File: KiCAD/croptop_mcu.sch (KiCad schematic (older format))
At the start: 46 parts

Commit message: Updates ESD protection diodes
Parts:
- removed TP?: TestPoint, symbol Connector:TestPoint
- added C17: 10uF, Capacitor_SMD:C_0805_2012Metric, symbol Device:C
- added FID1: FIDUCIAL, Fiducial:Fiducial_0.75mm_Dia_1.5mm_Outer, symbol CropTop:FIDUCIAL
- added FID2: FIDUCIAL, symbol CropTop:FIDUCIAL
- added H1: Top Left, symbol Mechanical:MountingHole
- added H2: Bottom Left, symbol Mechanical:MountingHole
- added H3: Top Right, symbol Mechanical:MountingHole
- added H4: Bottom Right, symbol Mechanical:MountingHole
- added R68, R69: 10, Resistor_SMD:R_0402_1005Metric, symbol Device:R
- added R70: 0, Resistor_SMD:R_0402_1005Metric, symbol Device:R
- added U16: PUSBM5V5X4, symbol CropTop:PUSBM5V5X4
- C1, C10, C11, C12, C13, C3, C4, C6, C7, C8, C9: renamed from C?; footprint (none) -> Capacitor_SMD:C_0402_1005Metric
- C2, C5: renamed from C?; footprint (none) -> Capacitor_SMD:C_0805_2012Metric
- R1, R10, R11, R12, R13, R14, R15, R16, R17, R18, R19, R2, R20, R21, R22, R23, R24, R25, R26, R27, R3, R4, R5, R6, R7, R8, R9: renamed from R?; footprint (none) -> Resistor_SMD:R_0402_1005Metric
- U1: renamed from U?; footprint MODULE -> Package_QFP:TQFP-100_12x12mm_P0.4mm
- gave numbers to parts that had none: 4
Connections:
- net labels added: ADC_CS, DVDD_UNREG, MISO, MOSI, RX, SCL, SCLK, SDA, TX
- net labels removed: GPS_RX, GPS_TX, MISO_1, MOSI_1, SCLK_1, SCL_1, SDA_1
- wire segments 248 -> 268
- no-connect marks 8 -> 12
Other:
- note added: "Mounting Holes & Fiducials"
- note removed: "Possibly\nD.N.P."
- note removed: "Supply \nmust\nbe 5V\nnot 3V3"
- moved on the sheet: C1, J1, J2, R1

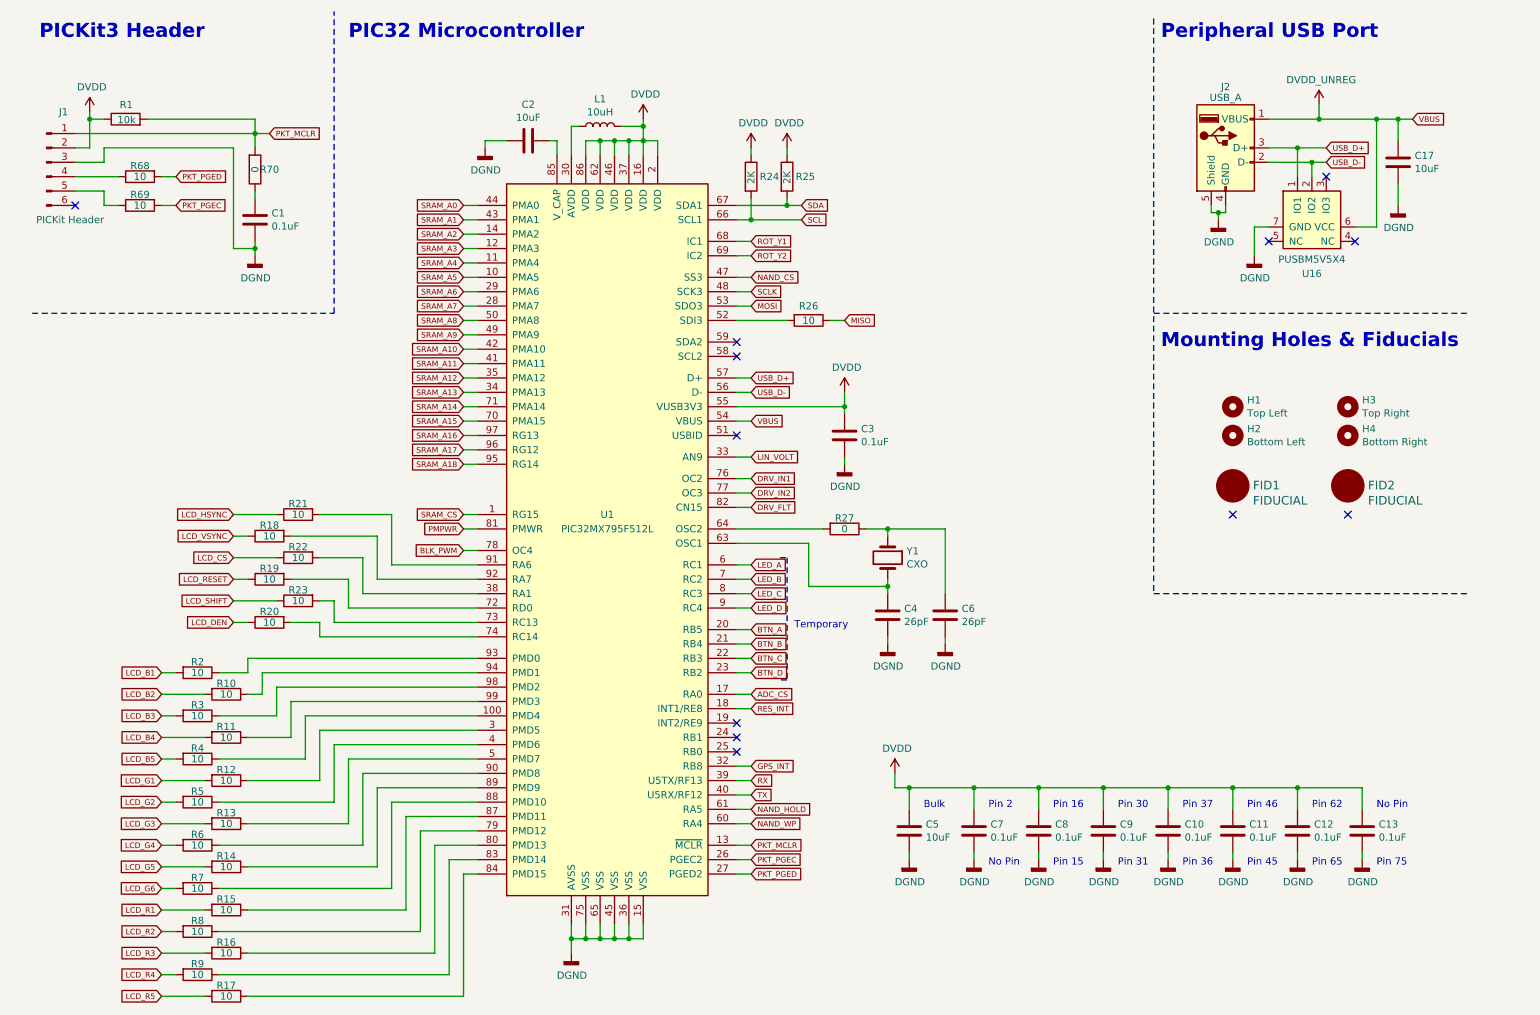
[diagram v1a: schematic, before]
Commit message: Got to PCB layout
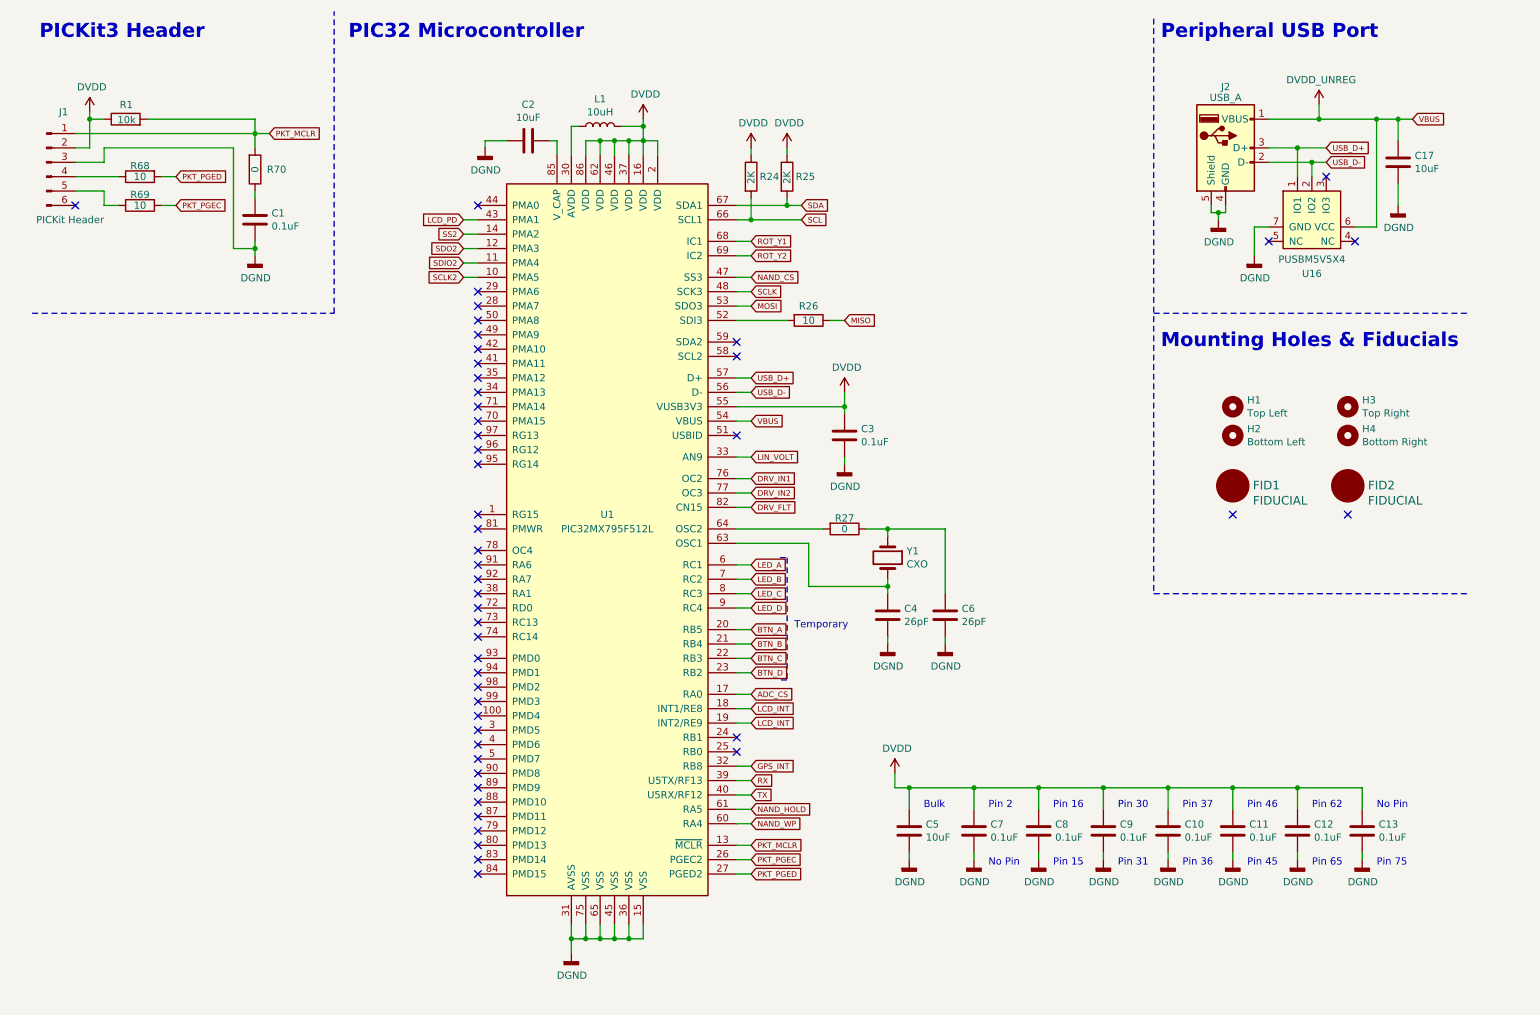
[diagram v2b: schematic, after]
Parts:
- removed R10, R11, R12, R13, R14, R15, R16, R17, R18, R19, R2, R20, R21, R22, R23, R3, R4, R5, R6, R7, R8, R9: 10, Resistor_SMD:R_0402_1005Metric, symbol Device:R
- FID1: footprint Fiducial:Fiducial_0.75mm_Dia_1.5mm_Outer -> Fiducial:Fiducial_1mm_Dia_2.54mm_Outer_CopperTop
- FID2: footprint (none) -> Fiducial:Fiducial_1mm_Dia_2.54mm_Outer_CopperTop
- H1, H2, H3, H4: footprint (none) -> MountingHole:MountingHole_4mm
- J1: footprint (none) -> Connector_PinHeader_2.54mm:PinHeader_1x06_P2.54mm_Vertical
- J2: footprint (none) -> croptop:USB_A_Assmann_Horizontal
- L1: footprint (none) -> Inductor_SMD:L_1210_3225Metric
- U16: footprint (none) -> croptop:PUSBM5V5X4
- Y1: footprint (none) -> croptop:ABLS_OX
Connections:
- net RES_INT is gone; now on net LCD_INT: U1.18 (INT1/RE8)
- net LCD_INT: now reaches U1.19 (INT2/RE9)
- net BLK_PWM: no longer names the net of U1.78 (OC4)
- net PMPWR: no longer names the net of U1.81 (PMWR)
- net SRAM_A0: no longer names the net of U1.44 (PMA0)
- net SRAM_A1 renamed LCD_PD
- net SRAM_A10: no longer names the net of U1.42 (PMA10)
- net SRAM_A11: no longer names the net of U1.41 (PMA11)
- net SRAM_A12: no longer names the net of U1.35 (PMA12)
- net SRAM_A13: no longer names the net of U1.34 (PMA13)
- net SRAM_A14: no longer names the net of U1.71 (PMA14)
- net SRAM_A15: no longer names the net of U1.70 (PMA15)
- net SRAM_A16: no longer names the net of U1.97 (RG13)
- net SRAM_A17: no longer names the net of U1.96 (RG12)
- net SRAM_A18: no longer names the net of U1.95 (RG14)
- net SRAM_A2 renamed SS2
- net SRAM_A3 renamed SDO2
- net SRAM_A4 renamed SDIO2
- net SRAM_A5 renamed SCLK2
- net SRAM_A6: no longer names the net of U1.29 (PMA6)
- net SRAM_A7: no longer names the net of U1.28 (PMA7)
- net SRAM_A8: no longer names the net of U1.50 (PMA8)
- net SRAM_A9: no longer names the net of U1.49 (PMA9)
- net SRAM_CS: no longer names the net of U1.1 (RG15)
- no-connect marks 12 -> 50

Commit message: Before remove LCD resistors
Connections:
- net BTN_C: no longer names the net of U1.22 (RB3)
- net BTN_D: no longer names the net of U1.23 (RB2)
- no-connect marks 50 -> 52
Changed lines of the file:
@@
 Text GLabel 5500 4900 2    39   Input ~ 0
 BTN_B
-Text GLabel 5500 5000 2    39   Input ~ 0
-BTN_C
-Text GLabel 5500 5100 2    39   Input ~ 0
-BTN_D
 Text GLabel 5500 4350 2    39   Input ~ 0
 LED_A
@@
 Wire Wire Line
 	5500 4900 5400 4900
-Wire Wire Line
-	5500 5000 5400 5000
-Wire Wire Line
-	5500 5100 5400 5100
 Wire Wire Line
 	5500 1800 5500 1950
@@
 Wire Wire Line
 	5400 5450 5500 5450
+NoConn ~ 5400 5000
+NoConn ~ 5400 5100
 $EndSCHEMATC

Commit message: Finished working board
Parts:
- removed R68, R69: 10, Resistor_SMD:R_0402_1005Metric, symbol Device:R
- H1, H2, H3, H4: footprint MountingHole:MountingHole_4mm -> MountingHole:MountingHole_4mm_Pad
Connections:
- net BTN_A: now also U1.74 (RC14); no longer U1.20 (RB5)
- net BTN_B: now also U1.73 (RC13); no longer U1.21 (RB4)
- net GPS_INT: now also U1.19 (INT2/RE9); no longer U1.32 (RB8)
- net LCD_INT: no longer U1.19 (INT2/RE9)
- net PKT_PGEC: now also J1.5 (Pin_5)
- net PKT_PGED: now also J1.4 (Pin_4)
- net LED_C: no longer names the net of U1.8 (RC3)
- net LED_D: no longer names the net of U1.9 (RC4)
- no-connect marks 52 -> 55
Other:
- note removed: "Temporary"
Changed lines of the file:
@@
 Wire Wire Line
 	4150 1400 4100 1400
-Text GLabel 5500 4800 2    39   Input ~ 0
+Text GLabel 3500 4850 0    39   Input ~ 0
 BTN_A
-Text GLabel 5500 4900 2    39   Input ~ 0
+Text GLabel 3500 4750 0    39   Input ~ 0
 BTN_B
 Text GLabel 5500 4350 2    39   Input ~ 0
@@
 Text GLabel 5500 4450 2    39   Input ~ 0
 LED_B
-Text GLabel 5500 4550 2    39   Input ~ 0
-LED_C
-Text GLabel 5500 4650 2    39   Input ~ 0
-LED_D
 $Comp
 L Device:R R?
@@
 	5400 2550 5500 2550
 Wire Wire Line
-	5500 4650 5400 4650
-Wire Wire Line
-	5500 4550 5400 4550
-Wire Wire Line
 	5500 4450 5400 4450
 Wire Wire Line
 	5500 4350 5400 4350
-Wire Wire Line
-	5500 4800 5400 4800
-Wire Wire Line
-	5500 4900 5400 4900
 Wire Wire Line
 	5500 1800 5500 1950
@@
 Wire Wire Line
 	6450 4100 6850 4100
-Text GLabel 10100 1250 2    39   Input ~ 0
-VBUS
-Text GLabel 5500 3350 2    39   Input ~ 0
-VBUS
-Wire Wire Line
-	5400 3350 5500 3350
 Wire Wire Line
 	6150 3150 6150 3250
@@
 Wire Wire Line
 	6050 2650 6150 2650
-Text GLabel 5500 5750 2    39   Input ~ 0
+Text GLabel 5500 5450 2    39   Input ~ 0
 GPS_INT
 Wire Wire Line
-	5400 5750 5500 5750
+	5400 5450 5500 5450
 Wire Wire Line
 	6300 4100 6450 4100
@@
 Text Notes 550  700  0    98   ~ 20
 PICKit3 Header
-Wire Notes Line
-	5700 4300 5750 4300
-Wire Notes Line
-	5750 4300 5750 5150
-Wire Notes Line
-	5750 5150 5700 5150
-Text Notes 5800 4800 0    50   ~ 0
-Temporary
 Wire Wire Line
 	9750 6350 9750 6400
@@
 F 0 "H1" H 8950 3296 50  0000 L CNN
 F 1 "Top Left" H 8950 3205 50  0000 L CNN
-F 2 "MountingHole:MountingHole_4mm" H 8850 3250 50  0001 C CNN
+F 2 "MountingHole:MountingHole_4mm_Pad" H 8850 3250 50  0001 C CNN
 F 3 "~" H 8850 3250 50  0001 C CNN
 	1    8850 3250
@@
 F 0 "H3" H 9750 3296 50  0000 L CNN
 F 1 "Top Right" H 9750 3205 50  0000 L CNN
-F 2 "MountingHole:MountingHole_4mm" H 9650 3250 50  0001 C CNN
+F 2 "MountingHole:MountingHole_4mm_Pad" H 9650 3250 50  0001 C CNN
 F 3 "~" H 9650 3250 50  0001 C CNN
 	1    9650 3250
@@
 F 0 "H2" H 8950 3496 50  0000 L CNN
 F 1 "Bottom Left" H 8950 3405 50  0000 L CNN
-F 2 "MountingHole:MountingHole_4mm" H 8850 3450 50  0001 C CNN
+F 2 "MountingHole:MountingHole_4mm_Pad" H 8850 3450 50  0001 C CNN
 F 3 "~" H 8850 3450 50  0001 C CNN
 	1    8850 3450
@@
 F 0 "H4" H 9750 3496 50  0000 L CNN
 F 1 "Bottom Right" H 9750 3405 50  0000 L CNN
-F 2 "MountingHole:MountingHole_4mm" H 9650 3450 50  0001 C CNN
+F 2 "MountingHole:MountingHole_4mm_Pad" H 9650 3450 50  0001 C CNN
 F 3 "~" H 9650 3450 50  0001 C CNN
 	1    9650 3450
@@
 NoConn ~ 8850 4000
 NoConn ~ 9650 4000
-$Comp
-L Device:R R?
-U 1 1 5C0298E7
-P 1250 1650
-AR Path="/5C0298E7" Ref="R?"  Part="1"
-AR Path="/64807BBC/5C0298E7" Ref="R68"  Part="1"
-F 0 "R68" V 1175 1650 50  0000 C CNN
-F 1 "10" V 1250 1650 50  0000 C CNN
-F 2 "Resistor_SMD:R_0402_1005Metric" V 1180 1650 50  0001 C CNN
-F 3 "~" H 1250 1650 50  0001 C CNN
-	1    1250 1650
-	0    -1   1    0
-$EndComp
-$Comp
-L Device:R R?
-U 1 1 5C08DA6B
-P 1250 1850
-AR Path="/5C08DA6B" Ref="R?"  Part="1"
-AR Path="/64807BBC/5C08DA6B" Ref="R69"  Part="1"
-F 0 "R69" V 1175 1850 50  0000 C CNN
-F 1 "10" V 1250 1850 50  0000 C CNN
-F 2 "Resistor_SMD:R_0402_1005Metric" V 1180 1850 50  0001 C CNN
-F 3 "~" H 1250 1850 50  0001 C CNN
-	1    1250 1850
-	0    -1   1    0
-$EndComp
 Wire Wire Line
 	800  1550 1000 1550
@@
 	1000 1550 1000 1450
 Wire Wire Line
-	800  1650 1100 1650
-Wire Wire Line
 	1000 1750 1000 1850
 Wire Wire Line
-	1000 1850 1100 1850
-Wire Wire Line
 	800  1750 1000 1750
 Wire Wire Line
@@
 Wire Wire Line
 	800  1350 2050 1350
-Wire Wire Line
-	1400 1650 1500 1650
-Wire Wire Line
-	1400 1850 1500 1850
 $Comp
 L Device:R R?
@@
 Wire Wire Line
 	10000 1400 10000 1250
-Connection ~ 10000 1250
-Wire Wire Line
-	10000 1250 10100 1250
 Wire Wire Line
 	10000 1700 10000 1850
@@
 NoConn ~ 3600 5100
 NoConn ~ 3600 5000
-NoConn ~ 3600 4850
-NoConn ~ 3600 4750
 NoConn ~ 3600 4650
 NoConn ~ 3600 4550
@@
 NoConn ~ 3600 2450
 NoConn ~ 3600 1850
-Text GLabel 5500 5450 2    39   Input ~ 0
-LCD_INT
 Text GLabel 3500 1950 0    39   Input ~ 0
 LCD_PD
 Wire Wire Line
 	3500 1950 3600 1950
-Wire Wire Line
-	5400 5450 5500 5450
 NoConn ~ 5400 5000
 NoConn ~ 5400 5100
+Wire Wire Line
+	800  1650 1500 1650
+Wire Wire Line
+	1000 1850 1500 1850
+NoConn ~ 5400 5750
+NoConn ~ 5400 4650
+NoConn ~ 5400 4550
+NoConn ~ 5400 4900
+NoConn ~ 5400 4800
+Wire Wire Line
+	3500 4750 3600 4750
+Wire Wire Line
+	3500 4850 3600 4850
+$Comp
+L CropTop:DVDD_UNREG #PWR?
+U 1 1 5C31543C
+P 5900 3000
+AR Path="/64809F0C/5C31543C" Ref="#PWR?"  Part="1"
+AR Path="/64807BBC/5C31543C" Ref="#PWR?"  Part="1"
+F 0 "#PWR?" H 5900 2850 50  0001 C CNN
+F 1 "DVDD_UNREG" H 5915 3173 50  0000 C CNN
+F 2 "" H 5900 3000 50  0001 C CNN
+F 3 "" H 5900 3000 50  0001 C CNN
+	1    5900 3000
+	1    0    0    -1
+$EndComp
+Wire Wire Line
+	5400 3350 5900 3350
+Wire Wire Line
+	5900 3350 5900 3000
 $EndSCHEMATC

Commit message: Complete PCB version 1
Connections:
- no-connect marks 55 -> 53
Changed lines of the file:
@@
 Wire Wire Line
 	5500 5250 5400 5250
-NoConn ~ 8850 4000
-NoConn ~ 9650 4000
 Wire Wire Line
 	800  1550 1000 1550
